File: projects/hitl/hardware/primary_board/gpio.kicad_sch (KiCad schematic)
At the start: 16 parts, among them J7 CONN_01X03, J8 CONN_01X03, Q3 SSM3K333R, Q4 SSM3K333R, U5 MAX7300AAXT

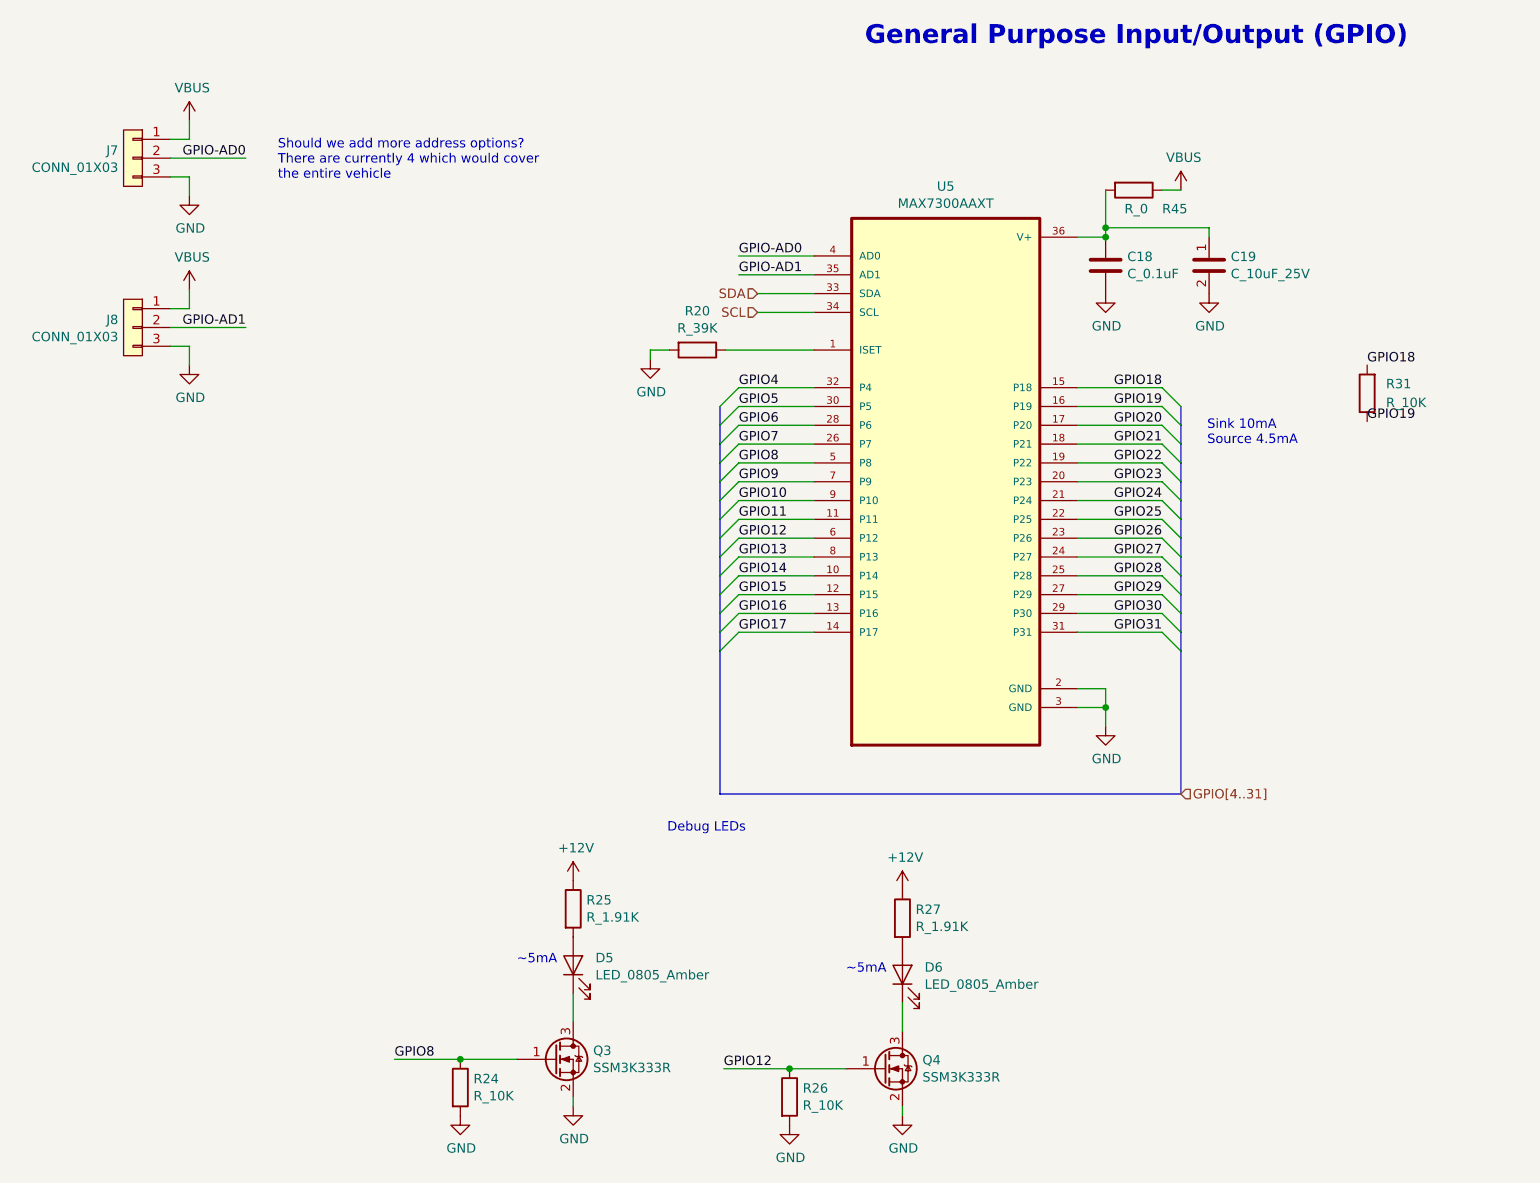
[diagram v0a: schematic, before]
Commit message: Replace zero-ohm resistors with solder jumpers
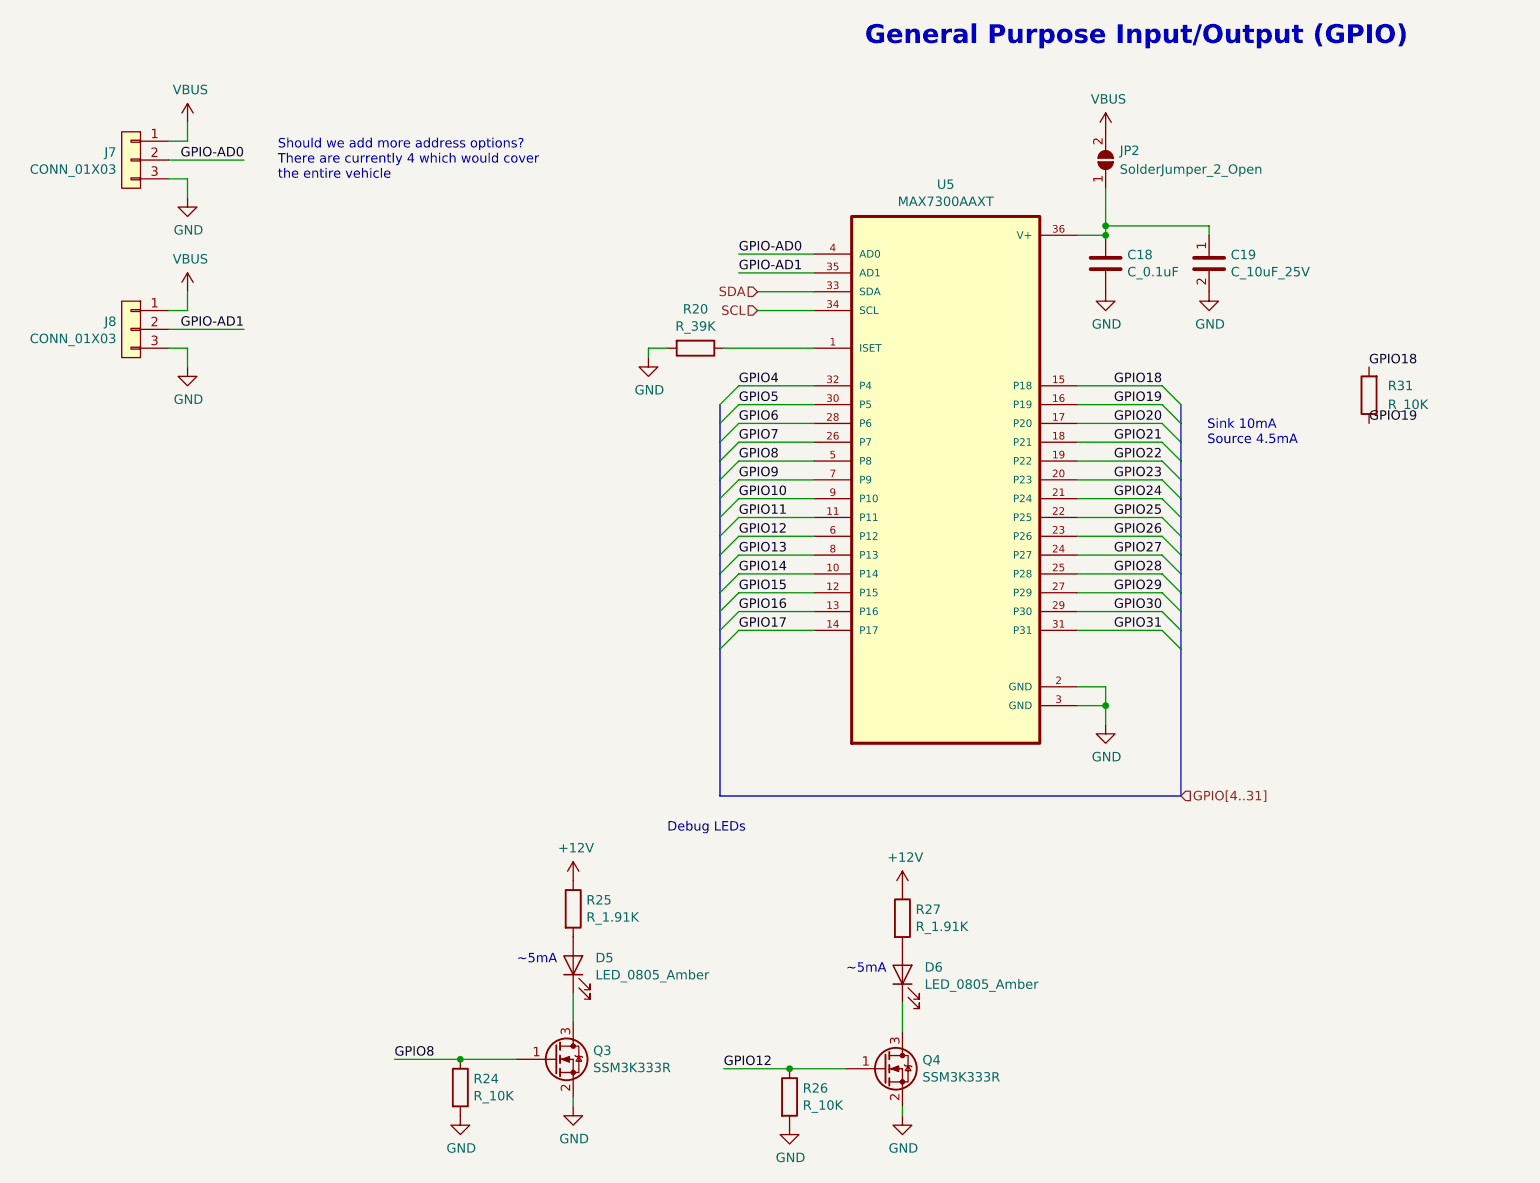
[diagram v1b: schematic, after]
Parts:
- removed R45: R_0, footprints:R_0603_1608Metric, symbol formula:R_0
- added JP2: SolderJumper_2_Open, Jumper:SolderJumper-2_P1.3mm_Open_RoundedPad1.0x1.5mm, symbol Jumper:SolderJumper_2_Open
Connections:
- net VBUS: now also JP2.2 (B)
- net at C18.1, C19.1, U5.36 (V+): now also JP2.1 (A)

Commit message: spec parts for hitl
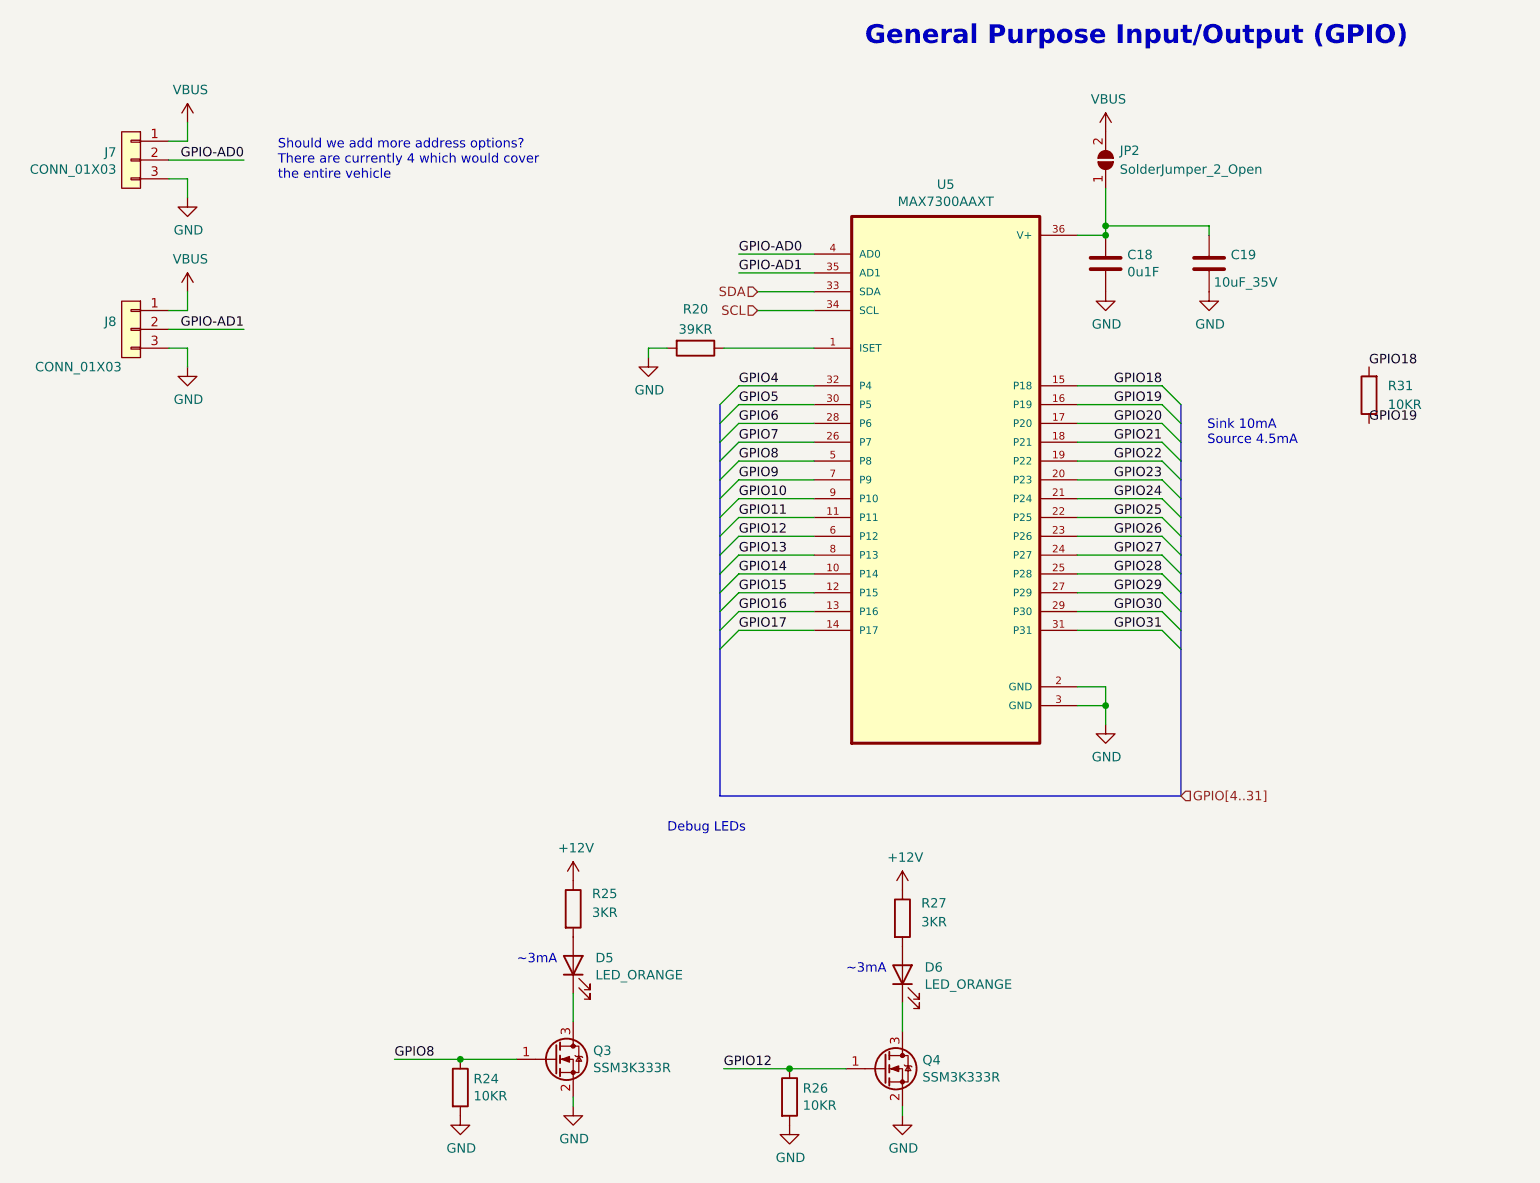
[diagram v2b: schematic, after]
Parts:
- C18: value C_0.1uF -> 0u1F; footprint footprints:C_0805_OEM -> OEM:C_0603; symbol formula:C_0.1uF -> OEM:0u1F; DKPN (none) -> 1276-1935-2-ND; MFN DK -> Samsung Electro-Mechanics; MPN 478-3352-1-ND -> CL10B104KB8NNWC; NewDesigns (none) -> YES; Package (none) -> 0603; PurchasingLink https://www.digikey.com/products/en?keywords=478-3352-1-ND -> (none); Stocked (none) -> Reel; Style (none) -> SMD
- C19: value C_10uF_25V -> 10uF_35V; footprint footprints:C_0805_OEM -> OEM:C_0603; symbol formula:C_10uF_25V -> OEM:10uF_35V; DKPN (none) -> 490-GRM188R6YA106MA73JDKR-ND; MFN (none) -> Murata; MPN (none) -> GRM188R6YA106MA73J; NewDesigns (none) -> YES; Package (none) -> 0603; Purchasing Link https://www.digikey.com/product-detail/en/murata-electronic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 -> (none); Stocked (none) -> Digi-Reel; Style (none) -> SMD
- D5, D6: value LED_0805_Amber -> LED_ORANGE; footprint footprints:LED_0805_OEM -> OEM:CHIPLED_0805; symbol formula:LED_0805_Amber -> OEM:LED_ORANGE; DKPN (none) -> 160-1413-6-ND; MFN DK -> Lite-On; MPN L71517CT-ND -> LTST-C170KFKT; NewDesigns (none) -> Yes; Package (none) -> 0805; PurchasingLink https://www.digikey.com/product-detail/en/visual-communicat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 -> (none); Stocked (none) -> Digi-Reel; Style (none) -> SMD
- J7, J8: symbol formula:CONN_01X03 -> OEM:CONN_01X03; DKPN (none) -> 2057-PH1-03-UA-ND; MFN Mouser -> Adam Tech; MPN 855-M20-9990346 -> PH1-03-UA; NewDesigns (none) -> YES; Package (none) -> .1" pin header; PurchasingLink https://www.mouser.com/ProductDetail/Harwin/M20-9990346?qs=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 -> (none); Stocked (none) -> Bulk; Style (none) -> THT
- JP2: now left out of the parts list
- Q3, Q4: footprint footprints:SOT-23F -> OEM:SOT-23F; symbol formula:SSM3K333R -> OEM:SSM3K333R; DKPN (none) -> SSM3K333RLFDKR-ND; MFN DK -> Toshiba; MPN SSM3K333RLFCT-ND -> SSM3K333R,LF; NewDesigns (none) -> YES; Package (none) -> SOT-23; PurchasingLink https://www.digikey.com/product-detail/en/toshiba-semicondu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 -> (none); Stocked (none) -> Digi-Reel; Style (none) -> SMD
- R20: value R_39K -> 39KR; footprint footprints:R_0805_OEM -> OEM:R_0603; symbol formula:R_39K -> OEM:39KR; DKPN (none) -> RMCF0603FT39K0DKR-ND; MFN TE -> Stackpole Electronics; MPN CRG0805F39K -> RMCF0603FT39K0; NewDesigns (none) -> YES; Package (none) -> 0603; PurchasingLink https://www.digikey.com/en/products/detail/te-connectivity-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 -> (none); Stocked (none) -> Reel; Style (none) -> SMD
- R24, R26, R31: value R_10K -> 10KR; footprint footprints:R_0805_OEM -> OEM:R_0603; symbol formula:R_10K -> OEM:10KR; DKPN (none) -> RMCF0603FT10K0TR-ND; MFN DK -> Stackpole Electronics; MPN CRS0805-FX-1002ELFCT-ND -> RMCF0603FT10K0; NewDesigns (none) -> YES; Package (none) -> 0603; PurchasingLink https://www.digikey.com/products/en?keywords=CRS0805-FX-100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 -> (none); Stocked (none) -> Reel; Style (none) -> SMD
- R25, R27: value R_1.91K -> 3KR; footprint footprints:R_0805_OEM -> OEM:R_0603; symbol formula:R_1.91K -> OEM:3KR; DKPN (none) -> 13-RC0603FR-103KLDKR-ND; MFN (none) -> Yageo; MPN (none) -> RC0603FR-103KL; NewDesigns (none) -> YES; Package (none) -> 0603; PurchasingLink https://www.digikey.com/product-detail/en/panasonic-electro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 -> (none); Stocked (none) -> Digi-Reel; Style (none) -> SMD
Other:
- note added: "~3mA"
- note removed: "~5mA"
